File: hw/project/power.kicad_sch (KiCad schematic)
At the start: 22 parts, among them Q1 SQM50061EL_GE3, Q2 SQM50061EL_GE3, U4 LMR51610XDBVR

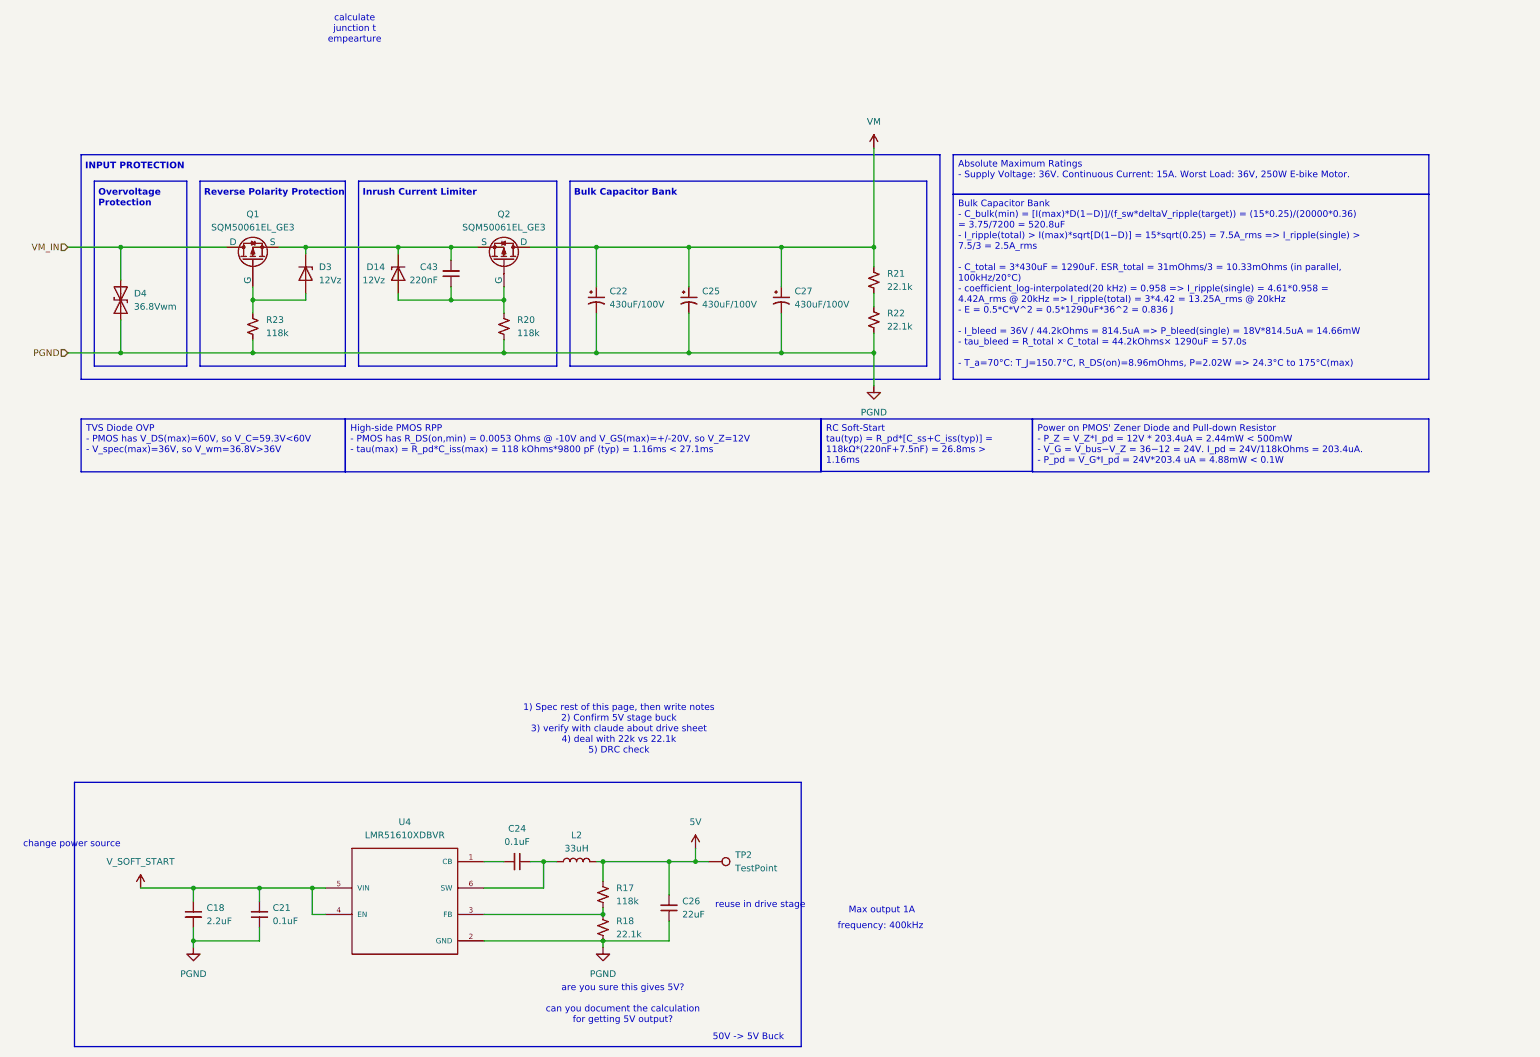
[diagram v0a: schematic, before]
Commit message: Finalize 5V buck regulator
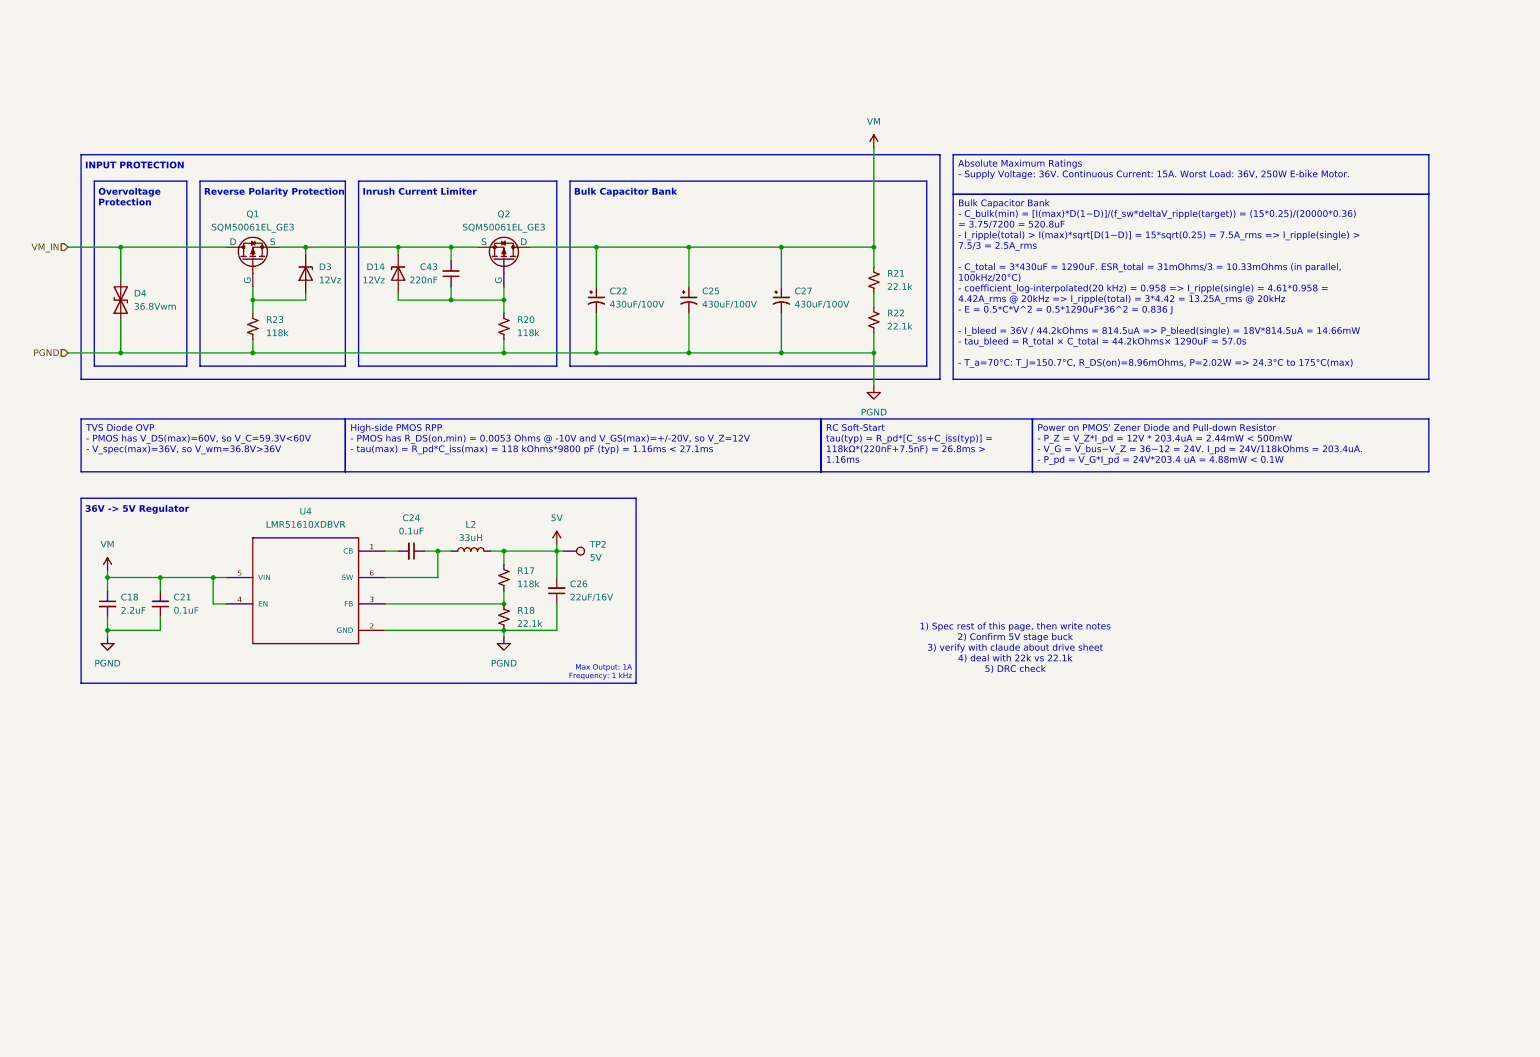
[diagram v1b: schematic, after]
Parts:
- C26: value 22uF -> 22uF/16V
- TP2: value TestPoint -> 5V
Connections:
- net V_SOFT_START is gone; now on net VM: C18.1, C21.2, U4.4 (EN), U4.5 (VIN)
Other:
- note added: "36V -> 5V Regulator"
- note added: "Max Output: 1A Frequency: 1 kHz"
- note removed: "50V -> 5V Buck"
- note removed: "Max output 1A"
- note removed: "are you sure this gives 5V? can you document the calculation for getting 5V output?"
- note removed: "calculate junction t empearture"
- note removed: "change power source"
- note removed: "frequency: 400kHz"
- note removed: "reuse in drive stage"
- moved on the sheet: C18, C21, C24, C26, L2, R17, R18, TP2, U4

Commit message: Finish speccing everything! Double-check stuff tomorrow
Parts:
- added TP10: VIN(5V), TestPoint:TestPoint_Pad_D1.0mm, symbol Connector:TestPoint
- added TP20: VM_IN, TestPoint:TestPoint_Pad_D1.0mm, symbol Connector:TestPoint
- added TP21: G(Q2), TestPoint:TestPoint_Pad_D1.0mm, symbol Connector:TestPoint
- added TP22: S(Q1/2), TestPoint:TestPoint_Pad_D1.0mm, symbol Connector:TestPoint
- added TP23: VM(bank), TestPoint:TestPoint_Pad_D1.0mm, symbol Connector:TestPoint
- TP2: value 5V -> VOUT(5V)
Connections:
- net VM: now also TP10.1, TP23.1
- net VM_IN: now also TP20.1
- net at C43.2, D14.1 (K), D3.1 (K)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: now also TP22.1
- net at C43.1, D14.2 (A), Q2.1 (G)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: now also TP21.1

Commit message: Fixed annotations and H-labels
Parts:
- TP12: renamed from TP20; now left out of the parts list
- TP13: renamed from TP22; now left out of the parts list
- TP14: renamed from TP23; now left out of the parts list
- TP15: renamed from TP21; now left out of the parts list
- TP16: renamed from TP2; now left out of the parts list
- TP17: renamed from TP10; now left out of the parts list
- renumbered C43 to C18, C22 to C19, C25 to C20, C27 to C21, C24 to C22, C26 to C23, C18 to C24, C21 to C25, D14 to D4, D4 to D5, R21 to R14, R22 to R15, R23 to R16, R20 to R17, R17 to R18, R18 to R19, U4 to U2
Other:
- note removed: "1) Spec rest of this page, then write notes 2) Confirm 5V stage buck 3) verify with claude about drive sheet 4) deal with 22k vs 22.1k 5) DRC check"

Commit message: Update shunt resistors and resolve ERC errors
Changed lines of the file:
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@@
+	(wire
+		(pts
+			(xy 104.14 95.25) (xy 104.14 96.52)
+		)
+		(stroke
+			(width 0)
+			(type default)
+		)
+	)
 	(wire
 		(pts
@@
 		(pts
 			(xy 139.7 38.1) (xy 139.7 45.72)
+		)
+		(stroke
+			(width 0)
+			(type default)
+		)
+	)
+	(wire
+		(pts
+			(xy 157.48 36.83) (xy 157.48 38.1)
 		)
 		(stroke
@@
 	(symbol
 		(lib_id "power:+5V")
-		(at 114.3 95.25 0)
+		(at 104.14 95.25 0)
 		(unit 1)
 		(body_style 1)
@@
 		(fields_autoplaced yes)
 		(property "Reference" "#PWR039"
-			(at 114.3 99.06 0)
+			(at 104.14 99.06 0)
 			(hide yes)
 			(show_name no)
@@
 		)
 		(property "Value" "5V"
-			(at 114.3 90.17 0)
+			(at 104.14 90.17 0)
 			(show_name no)
 			(do_not_autoplace no)
@@
 		)
 		(property "Footprint" ""
-			(at 114.3 95.25 0)
+			(at 104.14 95.25 0)
 			(hide yes)
 			(show_name no)
@@
 		)
 		(property "Datasheet" ""
-			(at 114.3 95.25 0)
+			(at 104.14 95.25 0)
 			(hide yes)
 			(show_name no)
@@
 		)
 		(property "Description" "Power symbol creates a global label with name \"+5V\""
-			(at 114.3 95.25 0)
+			(at 104.14 95.25 0)
 			(hide yes)
 			(show_name no)
@@
 				(path "/86a17c4d-db96-42a1-af84-d43fe593f4e6/5338eeb3-4021-4459-b70f-dab93d7c7a1a"
 					(reference "#PWR039")
+					(unit 1)
+				)
+			)
+		)
+	)
+	(symbol
+		(lib_id "power:PWR_FLAG")
+		(at 157.48 36.83 0)
+		(unit 1)
+		(body_style 1)
+		(exclude_from_sim no)
+		(in_bom yes)
+		(on_board yes)
+		(in_pos_files yes)
+		(dnp no)
+		(fields_autoplaced yes)
+		(property "Reference" "#FLG02"
+			(at 157.48 34.925 0)
+			(hide yes)
+			(show_name no)
+			(do_not_autoplace no)
+			(effects
+				(font
+					(size 1.27 1.27)
+				)
+			)
+		)
+		(property "Value" "PWR_FLAG"
+			(at 157.48 31.75 0)
+			(show_name no)
+			(do_not_autoplace no)
+			(effects
+				(font
+					(size 1.27 1.27)
+				)
+			)
+		)
+		(property "Footprint" ""
+			(at 157.48 36.83 0)
+			(hide yes)
+			(show_name no)
+			(do_not_autoplace no)
+			(effects
+				(font
+					(size 1.27 1.27)
+				)
+			)
+		)
+		(property "Datasheet" ""
+			(at 157.48 36.83 0)
+			(hide yes)
+			(show_name no)
+			(do_not_autoplace no)
+			(effects
+				(font
+					(size 1.27 1.27)
+				)
+			)
+		)
+		(property "Description" "Special symbol for telling ERC where power comes from"
+			(at 157.48 36.83 0)
+			(hide yes)
+			(show_name no)
+			(do_not_autoplace no)
+			(effects
+				(font
+					(size 1.27 1.27)
+				)
+			)
+		)
+		(pin "1"
+		)
+		(instances
+			(project "esc"
+				(path "/86a17c4d-db96-42a1-af84-d43fe593f4e6/5338eeb3-4021-4459-b70f-dab93d7c7a1a"
+					(reference "#FLG02")
 					(unit 1)
 				)
@@
 					(unit 1)
 				)
+			)
+		)
+	)
+	(symbol
+		(lib_id "power:PWR_FLAG")
+		(at 114.3 95.25 0)
+		(unit 1)
+		(body_style 1)
+		(exclude_from_sim no)
+		(in_bom yes)
+		(on_board yes)
+		(in_pos_files yes)
+		(dnp no)
+		(fields_autoplaced yes)
+		(property "Reference" "#FLG01"
+			(at 114.3 93.345 0)
+			(hide yes)
+			(show_name no)
+			(do_not_autoplace no)
+			(effects
+				(font
+					(size 1.27 1.27)
+				)
+			)
+		)
+		(property "Value" "PWR_FLAG"
+			(at 114.3 90.17 0)
+			(show_name no)
+			(do_not_autoplace no)
+			(effects
+				(font
+					(size 1.27 1.27)
+				)
+			)
+		)
+		(property "Footprint" ""
+			(at 114.3 95.25 0)
+			(hide yes)
+			(show_name no)
+			(do_not_autoplace no)
+			(effects
+				(font
+					(size 1.27 1.27)
+				)
+			)
+		)
+		(property "Datasheet" ""
+			(at 114.3 95.25 0)
+			(hide yes)
+			(show_name no)
+			(do_not_autoplace no)
+			(effects
+				(font
+					(size 1.27 1.27)
+				)
+			)
+		)
+		(property "Description" "Special symbol for telling ERC where power comes from"
+			(at 114.3 95.25 0)
+			(hide yes)
+			(show_name no)
+			(do_not_autoplace no)
+			(effects
+				(font
+					(size 1.27 1.27)
+				)
+			)
+		)
+		(pin "1"
+		)
+		(instances
+			(project "esc"
+				(path "/86a17c4d-db96-42a1-af84-d43fe593f4e6/5338eeb3-4021-4459-b70f-dab93d7c7a1a"
+					(reference "#FLG01")
+					(unit 1)
+				)

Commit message: Add drive sheet components and remove redundant components
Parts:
- C23: footprint Capacitor_SMD:C_0603_1608Metric -> Capacitor_SMD:C_0805_2012Metric
- C24: footprint Capacitor_SMD:C_1206_3216Metric -> Capacitor_SMD:C_0805_2012Metric
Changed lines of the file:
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@@
 			)
 		)
-		(property "Footprint" "Capacitor_SMD:C_1206_3216Metric"
+		(property "Footprint" "Capacitor_SMD:C_0805_2012Metric"
 			(at 27.94 106.68 0)
 			(hide yes)
@@
 			)
 		)
-		(property "Datasheet" "https://www.digikey.ca/en/products/detail/w%C3%BCrth-elektronik/885012208124/24721846"
+		(property "Datasheet" "https://www.digikey.ca/en/products/detail/murata-electronics/GRM21BD72A225ME01K/15972575"
 			(at 27.94 106.68 0)
 			(hide yes)
@@
 			)
 		)
-		(property "Description" "2.2 µF ±10% 100V Ceramic Capacitor X7R 1206 (3216 Metric)"
+		(property "Description" "CAP CER 2.2UF 100V X7T 0805"
 			(at 27.94 106.68 0)
 			(hide yes)
@@
 			)
 		)
-		(property "Footprint" "Capacitor_SMD:C_0603_1608Metric"
+		(property "Footprint" "Capacitor_SMD:C_0805_2012Metric"
 			(at 114.3 104.14 0)
 			(hide yes)
@@
 			)
 		)
-		(property "Datasheet" "https://www.digikey.ca/en/products/detail/samsung-electro-mechanics/CL10A226MO7JZNC/7320581"
+		(property "Datasheet" "https://www.digikey.ca/en/products/detail/samsung-electro-mechanics/CL21A226MAYNNWE/16344162"
 			(at 114.3 104.14 0)
 			(hide yes)
@@
 			)
 		)
-		(property "Description" "CAP CER 22UF 16V X5R 0603"
+		(property "Description" "CAP CER 22UF 25V X5R 0805"
 			(at 114.3 104.14 0)
 			(hide yes)
@@
 		(dnp no)
 		(fields_autoplaced yes)
-		(property "Reference" "#FLG02"
+		(property "Reference" "#FLG07"
 			(at 157.48 34.925 0)
 			(hide yes)
@@
 			(project "esc"
 				(path "/86a17c4d-db96-42a1-af84-d43fe593f4e6/5338eeb3-4021-4459-b70f-dab93d7c7a1a"
-					(reference "#FLG02")
+					(reference "#FLG07")
 					(unit 1)
 				)
@@
 		(dnp no)
 		(fields_autoplaced yes)
-		(property "Reference" "#FLG01"
+		(property "Reference" "#FLG08"
 			(at 114.3 93.345 0)
 			(hide yes)
@@
 			(project "esc"
 				(path "/86a17c4d-db96-42a1-af84-d43fe593f4e6/5338eeb3-4021-4459-b70f-dab93d7c7a1a"
-					(reference "#FLG01")
-					(unit 1)
-				)
+					(reference "#FLG08")
+					(unit 1)
+				)

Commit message: somewhat organize main groups
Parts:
- renumbered R14 to R11, R15 to R12, R16 to R13, R17 to R14, R18 to R15, R19 to R16
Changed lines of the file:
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@@
 		(dnp no)
 		(fields_autoplaced yes)
-		(property "Reference" "R18"
+		(property "Reference" "R15"
 			(at 106.68 100.3299 0)
 			(show_name no)
@@
 			(project "esc"
 				(path "/86a17c4d-db96-42a1-af84-d43fe593f4e6/5338eeb3-4021-4459-b70f-dab93d7c7a1a"
-					(reference "R18")
+					(reference "R15")
 					(unit 1)
 				)
@@
 		(dnp no)
 		(fields_autoplaced yes)
-		(property "Reference" "R19"
+		(property "Reference" "R16"
 			(at 106.68 107.9499 0)
 			(show_name no)
@@
 			(project "esc"
 				(path "/86a17c4d-db96-42a1-af84-d43fe593f4e6/5338eeb3-4021-4459-b70f-dab93d7c7a1a"
-					(reference "R19")
+					(reference "R16")
 					(unit 1)
 				)
@@
 		(dnp no)
 		(fields_autoplaced yes)
-		(property "Reference" "R15"
+		(property "Reference" "R12"
 			(at 177.8 50.7999 0)
 			(show_name no)
@@
 			(project "esc"
 				(path "/86a17c4d-db96-42a1-af84-d43fe593f4e6/5338eeb3-4021-4459-b70f-dab93d7c7a1a"
-					(reference "R15")
+					(reference "R12")
 					(unit 1)
 				)
@@
 		(dnp no)
 		(fields_autoplaced yes)
-		(property "Reference" "R17"
+		(property "Reference" "R14"
 			(at 106.68 52.0699 0)
 			(show_name no)
@@
 			(project "esc"
 				(path "/86a17c4d-db96-42a1-af84-d43fe593f4e6/5338eeb3-4021-4459-b70f-dab93d7c7a1a"
-					(reference "R17")
+					(reference "R14")
 					(unit 1)
 				)
@@
 		(dnp no)
 		(fields_autoplaced yes)
-		(property "Reference" "R16"
+		(property "Reference" "R13"
 			(at 58.42 52.0699 0)
 			(show_name no)
@@
 			(project "esc"
 				(path "/86a17c4d-db96-42a1-af84-d43fe593f4e6/5338eeb3-4021-4459-b70f-dab93d7c7a1a"
-					(reference "R16")
+					(reference "R13")
 					(unit 1)
 				)
@@
 		(dnp no)
 		(fields_autoplaced yes)
-		(property "Reference" "R14"
+		(property "Reference" "R11"
 			(at 177.8 43.1799 0)
 			(show_name no)
@@
 			(project "esc"
 				(path "/86a17c4d-db96-42a1-af84-d43fe593f4e6/5338eeb3-4021-4459-b70f-dab93d7c7a1a"
-					(reference "R14")
-					(unit 1)
-				)
+					(reference "R11")
+					(unit 1)
+				)

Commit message: Place critical components near MCU
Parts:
- renumbered R11 to R10, R12 to R11, R13 to R12, R14 to R13, R15 to R14, R16 to R15
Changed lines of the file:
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@@
 		(dnp no)
 		(fields_autoplaced yes)
-		(property "Reference" "R15"
+		(property "Reference" "R14"
 			(at 106.68 100.3299 0)
 			(show_name no)
@@
 			(project "esc"
 				(path "/86a17c4d-db96-42a1-af84-d43fe593f4e6/5338eeb3-4021-4459-b70f-dab93d7c7a1a"
-					(reference "R15")
+					(reference "R14")
 					(unit 1)
 				)
@@
 		(dnp no)
 		(fields_autoplaced yes)
-		(property "Reference" "R16"
+		(property "Reference" "R15"
 			(at 106.68 107.9499 0)
 			(show_name no)
@@
 			(project "esc"
 				(path "/86a17c4d-db96-42a1-af84-d43fe593f4e6/5338eeb3-4021-4459-b70f-dab93d7c7a1a"
-					(reference "R16")
+					(reference "R15")
 					(unit 1)
 				)
@@
 		(dnp no)
 		(fields_autoplaced yes)
-		(property "Reference" "R12"
+		(property "Reference" "R11"
 			(at 177.8 50.7999 0)
 			(show_name no)
@@
 			(project "esc"
 				(path "/86a17c4d-db96-42a1-af84-d43fe593f4e6/5338eeb3-4021-4459-b70f-dab93d7c7a1a"
-					(reference "R12")
+					(reference "R11")
 					(unit 1)
 				)
@@
 		(dnp no)
 		(fields_autoplaced yes)
-		(property "Reference" "R14"
+		(property "Reference" "R13"
 			(at 106.68 52.0699 0)
 			(show_name no)
@@
 			(project "esc"
 				(path "/86a17c4d-db96-42a1-af84-d43fe593f4e6/5338eeb3-4021-4459-b70f-dab93d7c7a1a"
-					(reference "R14")
+					(reference "R13")
 					(unit 1)
 				)
@@
 		(dnp no)
 		(fields_autoplaced yes)
-		(property "Reference" "R13"
+		(property "Reference" "R12"
 			(at 58.42 52.0699 0)
 			(show_name no)
@@
 			(project "esc"
 				(path "/86a17c4d-db96-42a1-af84-d43fe593f4e6/5338eeb3-4021-4459-b70f-dab93d7c7a1a"
-					(reference "R13")
+					(reference "R12")
 					(unit 1)
 				)
@@
 		(dnp no)
 		(fields_autoplaced yes)
-		(property "Reference" "R11"
+		(property "Reference" "R10"
 			(at 177.8 43.1799 0)
 			(show_name no)
@@
 			(project "esc"
 				(path "/86a17c4d-db96-42a1-af84-d43fe593f4e6/5338eeb3-4021-4459-b70f-dab93d7c7a1a"
-					(reference "R11")
-					(unit 1)
-				)
+					(reference "R10")
+					(unit 1)
+				)
